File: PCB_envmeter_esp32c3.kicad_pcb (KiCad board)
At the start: 2 copper layers, 72 x 47.5 mm, 25 parts, among them J1 USB_C_Receptacle_USB2.0_16P, J3 AE-BME680, J4 SSD1306, SW1 Reset, SW2 Mode, U1 ESP32-C3-WROOM-02, U2 AP7333-33SAG, U3 NJM2845DL1-33

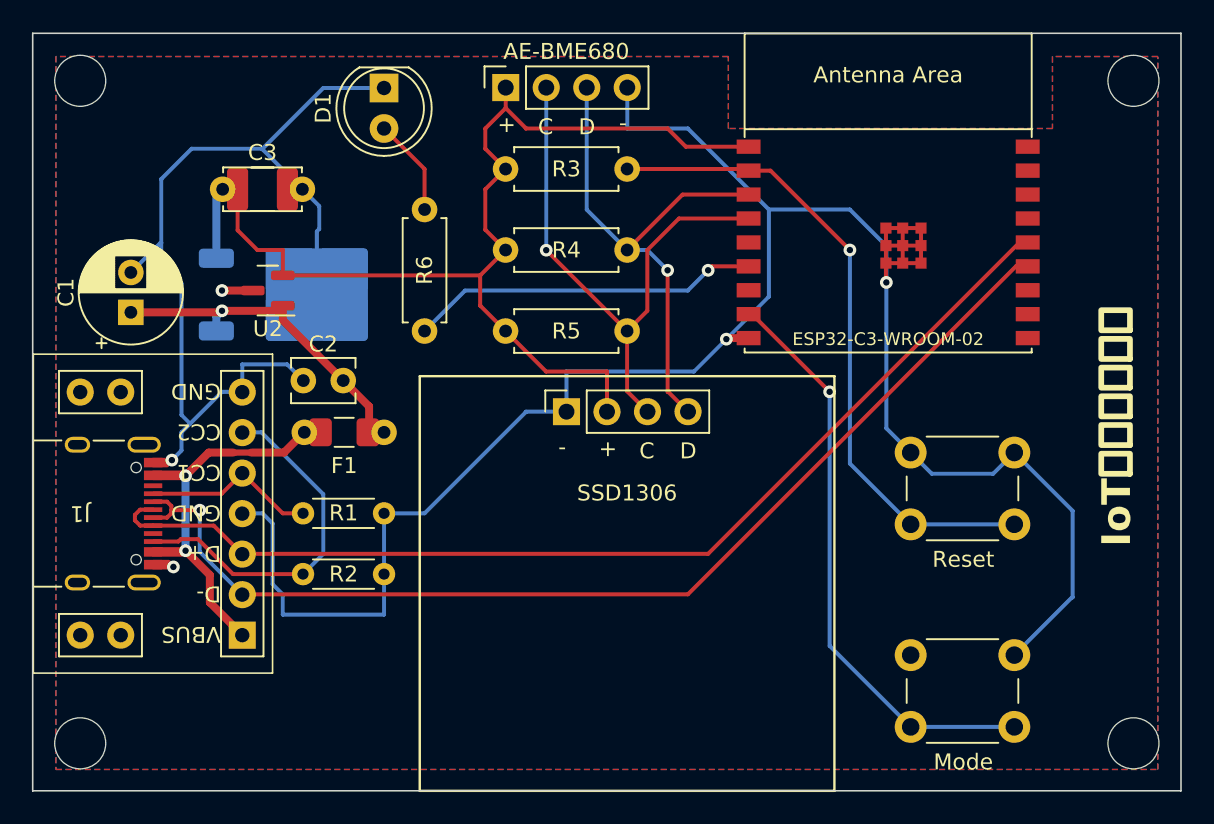
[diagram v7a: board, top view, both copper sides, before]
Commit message: Rev. 2
* スマートリモコン機能追加
  - 赤外線送信部
  - 赤外線受信部
* AE-BME680とSSD1306のパッド穴サイズを1.0mmから0.9mmに変更
* JLCJLCJLCJLC を WayWayWay に変更
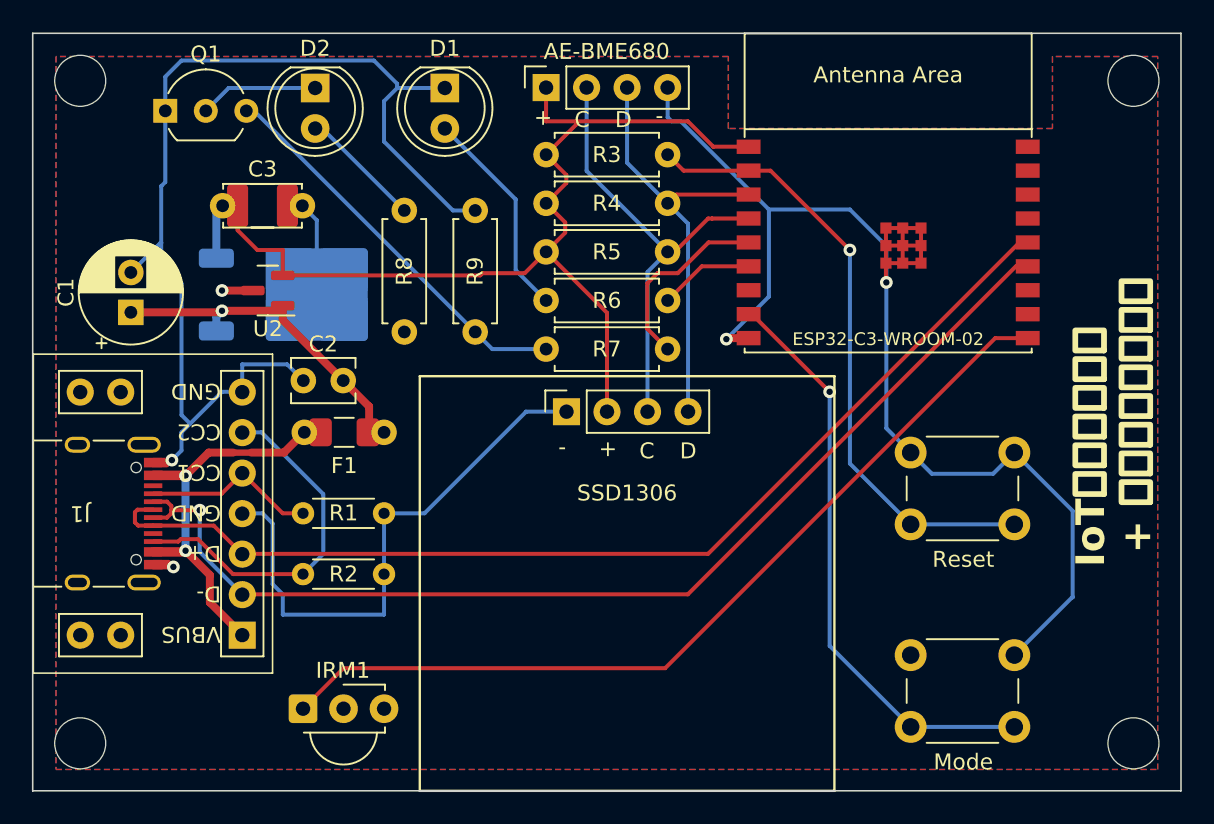
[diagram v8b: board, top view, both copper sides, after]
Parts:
- added D2: LED, LED_THT:LED_D5.0mm_IRGrey, F.Cu at (52.8, 38.1)
- added IRM1: OSRB38C9AA, OptoDevice:Vishay_MINICAST-3Pin, F.Cu at (52.1, 77.0)
- added Q1: 2SC2001, Package_TO_SOT_THT:TO-92_Inline_Wide, F.Cu at (43.4, 39.5)
- added R7: 680, Resistor_THT:R_Axial_DIN0207_L6.3mm_D2.5mm_P7.62mm_Horizontal, F.Cu at (74.9, 54.5)
- added R8: 5.1, Resistor_THT:R_Axial_DIN0207_L6.3mm_D2.5mm_P7.62mm_Horizontal, F.Cu at (58.4, 53.4)
- added R9: 4.7k, Resistor_THT:R_Axial_DIN0207_L6.3mm_D2.5mm_P7.62mm_Horizontal, F.Cu at (62.9, 53.4)
- moved R6 15.4 mm to (74.9, 51.4), turned to 180 degrees
- moved R5 5.58 mm to (67.3, 48.4)
- moved R4 3.88 mm to (67.3, 45.3)
- moved D1 3.81 mm to (61.0, 38.1)
- moved R3 2.69 mm to (67.3, 42.3)
- moved J3 2.53 mm to (67.3, 38.1)
- moved C3 1.03 mm to (49.5, 45.5)
- moved C4 1.03 mm to (47.0, 45.5)
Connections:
- U1 pad 10: unconnected-(U1-GPIO10-Pad10) -> IRin
- U1 pad 5: unconnected-(U1-GPIO6-Pad5) -> IRout
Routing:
- net IRin: track 0.00 -> 55.1 mm
- net Net-(Q1-B): track 0.00 -> 25.0 mm
- net Net-(U1-GPIO7): track 22.0 -> 5.97 mm, vias 1 -> 0
- net IRout: track 0.00 -> 12.1 mm
- net Net-(D2-A): track 0.00 -> 7.72 mm
- net Net-(D2-K): track 0.00 -> 7.45 mm
- net Net-(D1-A): track 6.13 -> 13.4 mm
- net SCL: track 35.7 -> 29.1 mm, vias 1 -> 0
- net SDA: track 32.8 -> 27.2 mm, vias 1 -> 0
- net +3.3V: track 69.2 -> 66.2 mm
- net Net-(U1-EN/CHIP_PU): track 41.4 -> 39.2 mm
- net GND: track 198.1 -> 197.3 mm
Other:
- board text added: "IoT環境メーター + スマートリモコン"
- board text added: "WayWayWay"
- board text removed: "IoT環境メーター"
- board text removed: "JLCJLCJLCJLC"
